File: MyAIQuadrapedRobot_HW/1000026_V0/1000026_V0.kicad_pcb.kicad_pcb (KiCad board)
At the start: 4 copper layers, 100 x 70 mm, 27 parts, among them J2 0525591853, J3 532580229, J5 532580229, J7 533750410, J9 0525591853, SW1 TL3305CF260QG, U1 TXB0108PWR, U2 MAX7480ESA+

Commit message: Development changes.
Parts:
- A1, A2: footprint CatBot_JSC:Arduino_BLE_33 -> myKiCadGlobalFootprintLibrary:Nano33BLE_with_headers
- H1, H2, H3, H4: footprint MountingHole:MountingHole_2.2mm_M2 -> myKiCadGlobalFootprintLibrary:MountingHole_2.2mm_M2
- R1: footprint CatBot_JSC:300_Ohm_RESC6332X70N -> myKiCadGlobalFootprintLibrary:RESC6332X70N
- SW1: footprint CatBot_JSC:Push_Button_Switch_SW4_TL3305CF260QG_EWI-M -> myKiCadGlobalFootprintLibrary:TL3305CF260QG
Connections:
- net Net-(A1-Pad22) renamed PB
- J9 pad 17: unconnected-(J9-Pad17) -> GND
- J9 pad 18: unconnected-(J9-Pad18) -> 3.3V_1
- R1 pad 1: Net-(LED1-Pad2) -> 7.4V
- R1 pad 2: 7.4V -> Net-(LED1-Pad2)
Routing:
- net Net-(LED1-Pad2): track 10.7 -> 0.00 mm, vias 1 -> 0
- net 7.4V: track 257.0 -> 267.6 mm, vias 3 -> 4

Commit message: Update of KiCad library in progress.
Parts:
- removed C6: CL05A104KA5NNNC_0pt1uF, CatBot_JSC:CAPC1005X55N
- added C4: CL05A104KA5NNNC, myKiCadGlobalFootprintLibrary:CAPC1005X55N, F.Cu at (152.3, 55.1)
- C1: value CL05A104KA5NNNC_0pt1uF -> 12065C503JAT2A; footprint CatBot_JSC:CAPC1005X55N -> myKiCadGlobalFootprintLibrary:12065C503JAT2A
- C2, C3: value CL05A104KA5NNNC_0pt1uF -> CL05A104KA5NNNC; footprint CatBot_JSC:CAPC1005X55N -> myKiCadGlobalFootprintLibrary:CAPC1005X55N
- C5: value CL05A104KA5NNNC_0pt1uF -> CL05A104KA5NNNC; footprint CatBot_JSC:CAPC1005X55N -> myKiCadGlobalFootprintLibrary:CAPC1005X55N; moved to F.Cu
- D1, D2, D3: footprint CatBot_JSC:Diode_CR_SOD323_MCC-M -> myKiCadGlobalFootprintLibrary:1N4148WT
- F1: footprint CatBot_JSC:RGEF300 -> myKiCadGlobalFootprintLibrary:RGEF300HF
- J3, J5: footprint Molex_connectors_JSC:CON_532580229_MOL -> myKiCadGlobalFootprintLibrary:0532580229
- LED1: footprint CatBot_JSC:Led_green_C503B -> myKiCadGlobalFootprintLibrary:C503B-GAN-CB0F0791
- R2: footprint CatBot_JSC:RC0402JR-0710KL -> myKiCadGlobalFootprintLibrary:RC0402JR-0710KL
- S1: footprint CatBot_JSC:Slider_switch_500SSP1S2M2QEA -> myKiCadGlobalFootprintLibrary:500SSP1S2M2QEA
- U2: footprint CatBot_JSC:SOIC127P600X175-8N_MAX7480 -> myKiCadGlobalFootprintLibrary:MAX7480ESA
- moved C5 11.9 mm to (140.6, 57.1), turned to 180 degrees
- moved C1 0.72 mm to (155.6, 55.9), turned to 90 degrees
- moved D1 0.56 mm to (157.7, 115.5)
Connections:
- C1 pad 1: /CLK -> GND
- C1 pad 2: GND -> /CLK
- C5 pad 1: 5V_1 -> /COM
- U2 pad 4: 5V_1 -> GND
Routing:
- net Net-(LED1-Pad2): track 0.00 -> 10.7 mm, vias 0 -> 1
- net 7.4V: track 267.6 -> 257.0 mm, vias 4 -> 3
- net GND: track 374.6 -> 376.2 mm
- net PWM: track 35.8 -> 37.0 mm
- net /CLK: track 18.2 -> 17.3 mm

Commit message: KiCad library update complete.
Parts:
- removed J7: 533750410, Molex_connectors_JSC:MOLEX_533750410
- added J1: 533750410, myKiCadGlobalFootprintLibrary:533750410, F.Cu at (183.3, 114.0)
- J2, J9: footprint Molex_connectors_JSC:CON_525591853_MOL -> myKiCadGlobalFootprintLibrary:525591853
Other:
- board text added: "*(7.4V fused)*"
- board text added: "*(GND)*"
- board text removed: "(7.4V fused)"
- board text removed: "(GND)"

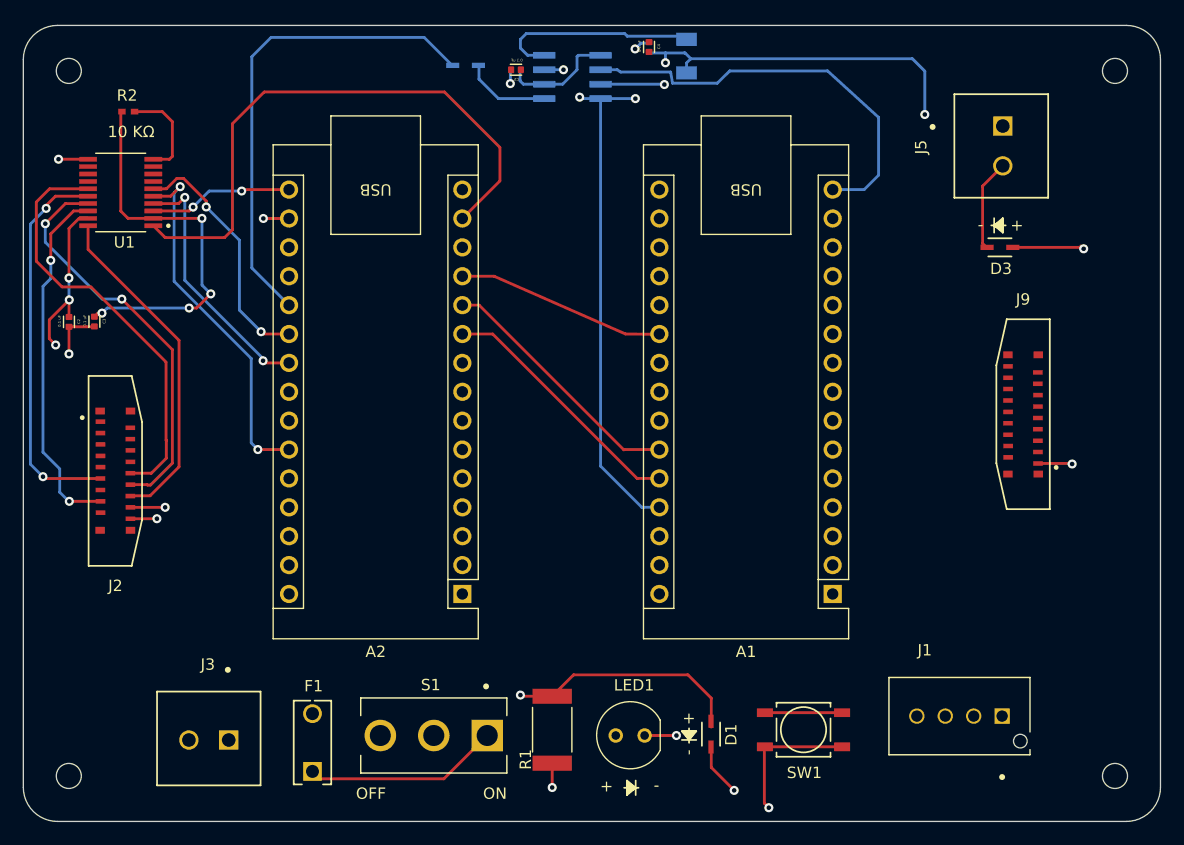
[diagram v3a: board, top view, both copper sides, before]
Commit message: All tracks in place but needs improvement.
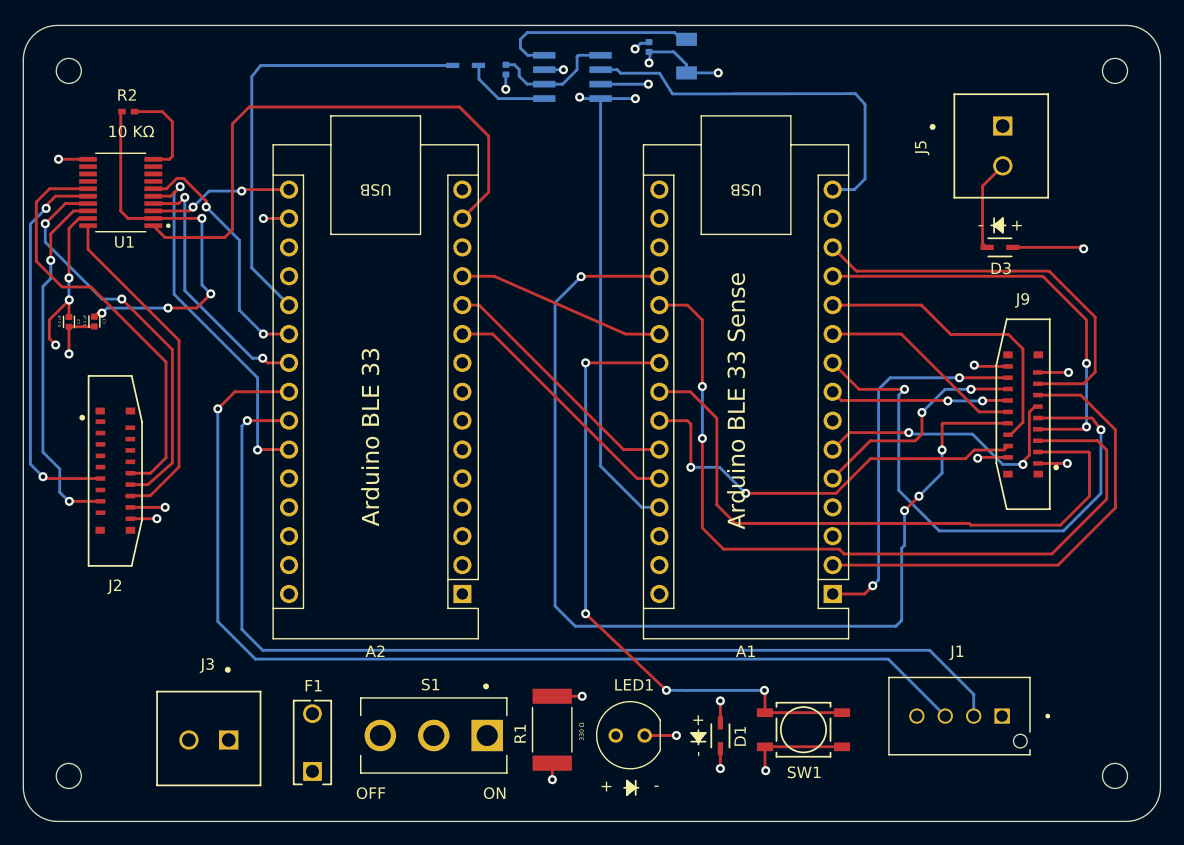
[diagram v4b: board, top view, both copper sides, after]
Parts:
- C4, C5: moved to B.Cu
- moved C5 0.88 mm to (139.7, 57.1), turned to -90 degrees
- moved D1 0.84 mm to (158.5, 115.7)
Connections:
- A1 pad 1: unconnected-(A1-Pad1) -> D1
- A1 pad 10: unconnected-(A1-Pad10) -> D7
- A1 pad 11: unconnected-(A1-Pad11) -> VSYNC
- A1 pad 12: unconnected-(A1-Pad12) -> XCLK
- A1 pad 13: unconnected-(A1-Pad13) -> D0
- A1 pad 19: unconnected-(A1-Pad19) -> PCLK
- A1 pad 2: unconnected-(A1-Pad2) -> D2
- A1 pad 20: unconnected-(A1-Pad20) -> HS
- A1 pad 23: SDA -> SDA_1
- A1 pad 24: SDL -> SCL_1
- A1 pad 5: unconnected-(A1-Pad5) -> D3
- A1 pad 6: unconnected-(A1-Pad6) -> D4
- A1 pad 8: unconnected-(A1-Pad8) -> D5
- A1 pad 9: unconnected-(A1-Pad9) -> D6
- A2 pad 23: unconnected-(A2-Pad23) -> SDA_2
- A2 pad 24: unconnected-(A2-Pad24) -> SDL_2
- J1 pad 2: SDL -> SDL_2
- J1 pad 3: SDA -> SDA_2
- J9 pad 10: unconnected-(J9-Pad10) -> D7
- J9 pad 11: unconnected-(J9-Pad11) -> D4
- J9 pad 12: unconnected-(J9-Pad12) -> D5
- J9 pad 13: unconnected-(J9-Pad13) -> D2
- J9 pad 14: unconnected-(J9-Pad14) -> D3
- J9 pad 15: unconnected-(J9-Pad15) -> D0
- J9 pad 16: unconnected-(J9-Pad16) -> D1
- J9 pad 3: unconnected-(J9-Pad3) -> SDA_1
- J9 pad 4: unconnected-(J9-Pad4) -> SCL_1
- J9 pad 5: unconnected-(J9-Pad5) -> HS
- J9 pad 6: unconnected-(J9-Pad6) -> VSYNC
- J9 pad 7: unconnected-(J9-Pad7) -> XCLK
- J9 pad 8: unconnected-(J9-Pad8) -> PCLK
- J9 pad 9: unconnected-(J9-Pad9) -> D6
- U2 pad 4: GND -> 5V_1
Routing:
- net 3.3V_1: track 0.00 -> 116.7 mm, vias 0 -> 2
- net SDA_2: track 0.00 -> 93.0 mm, vias 0 -> 1
- net PCLK: track 0.00 -> 92.9 mm, vias 0 -> 4
- net SDL_2: track 0.00 -> 90.9 mm, vias 0 -> 1
- net HS: track 0.00 -> 71.8 mm, vias 0 -> 2
- net SDA_1: track 0.00 -> 56.6 mm
- net PB: track 6.88 -> 55.8 mm, vias 0 -> 4
- net D6: track 0.00 -> 48.7 mm, vias 0 -> 2
- net D2: track 0.00 -> 41.9 mm
- net XCLK: track 0.00 -> 37.7 mm, vias 0 -> 2
- net SCL_1: track 0.00 -> 37.2 mm, vias 0 -> 2
- net D0: track 0.00 -> 35.9 mm
- net D1: track 0.00 -> 33.1 mm, vias 0 -> 2
- net VSYNC: track 0.00 -> 26.6 mm
- net 7.4V: track 257.0 -> 232.0 mm, vias 3 -> 4
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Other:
- board text added: "Arduino BLE 33"
- board text added: "Arduino BLE 33 Sense"

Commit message: Clean up of tracks in progress.
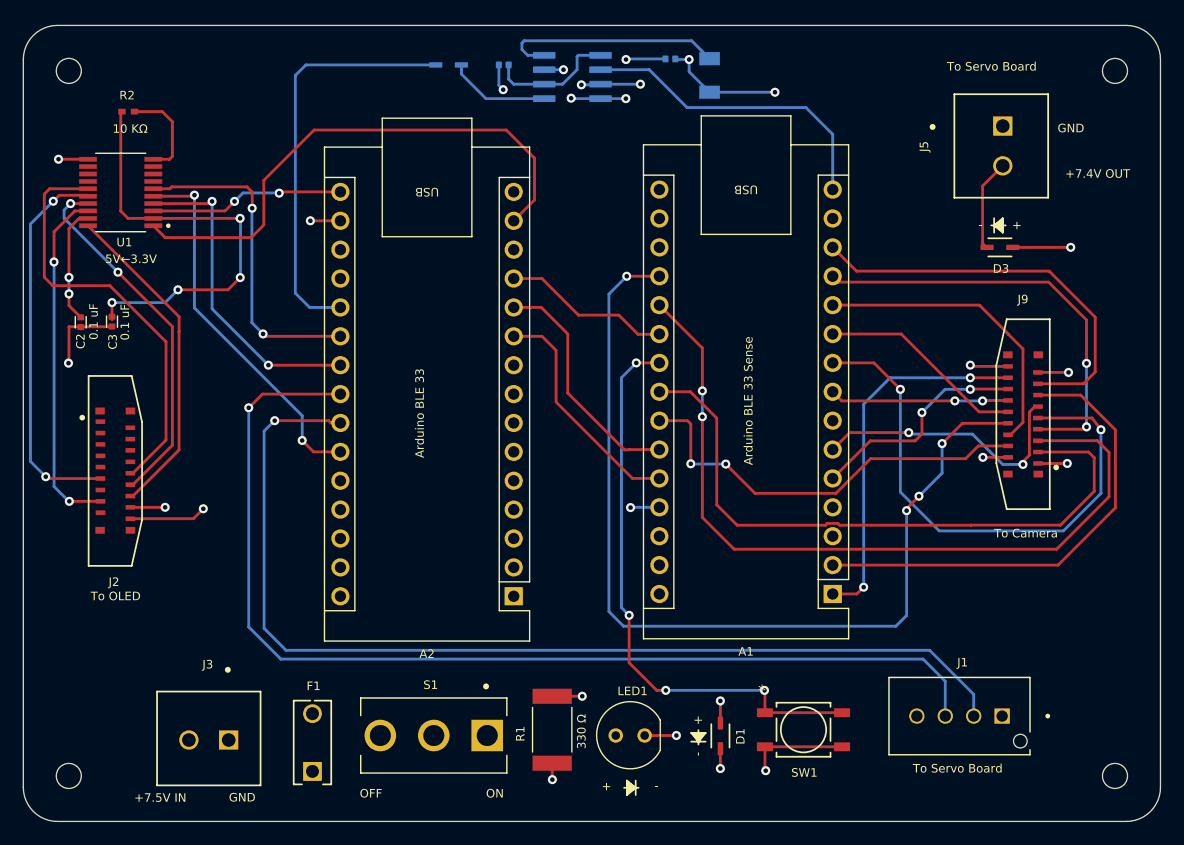
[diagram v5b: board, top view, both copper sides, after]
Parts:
- moved A2 4.52 mm to (140.4, 103.4)
- moved C1 2.64 mm to (157.6, 57.6)
- moved C4 2.15 mm to (154.1, 56.2), turned to 0 degrees
- moved C3 1.55 mm to (105.0, 79.3)
- moved D2 1.49 mm to (134.6, 56.7)
- moved C2 1.03 mm to (102.3, 79.3)
- moved C5 0.46 mm to (139.5, 56.7), turned to 180 degrees
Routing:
- net 7.4V: track 232.0 -> 211.3 mm
- net 3.3V_1: track 116.7 -> 100.8 mm
- net PCLK: track 92.9 -> 83.1 mm
- net 5V_2: track 48.0 -> 57.8 mm, vias 4 -> 3
- net PWM: track 34.6 -> 27.6 mm
- net CS: track 21.9 -> 28.7 mm
- net 3.3V_2: track 41.8 -> 47.3 mm
- net DC: track 23.0 -> 28.0 mm
- net PB: track 55.8 -> 51.0 mm
- net SCK: track 12.7 -> 17.2 mm
- net bit_2: track 18.4 -> 14.9 mm
- net DC_5V: track 35.6 -> 32.1 mm
- net Analog: track 39.5 -> 36.4 mm
- net /CLK: track 17.8 -> 20.0 mm
- net HS: track 71.8 -> 69.6 mm
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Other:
- board text added: "+7.4V OUT"
- board text added: "+7.5V IN"
- board text added: "1000026_V0a Copyright © James Canova, June 2023, Victoria, BC Canada"
- board text added: "5V←3.3V"
- board text added: "GND"
- board text added: "PWM → DC (low pass filter)"
- board text added: "To Camera"
- board text added: "To OLED"
- board text added: "To Servo Board"
